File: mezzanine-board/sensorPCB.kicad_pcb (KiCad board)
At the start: 2 copper layers, 50.8 x 8 mm, 23 parts, among them J2 20021311-00020T4LF, U3 AS72652, U4 AS72653, U6 AS72651

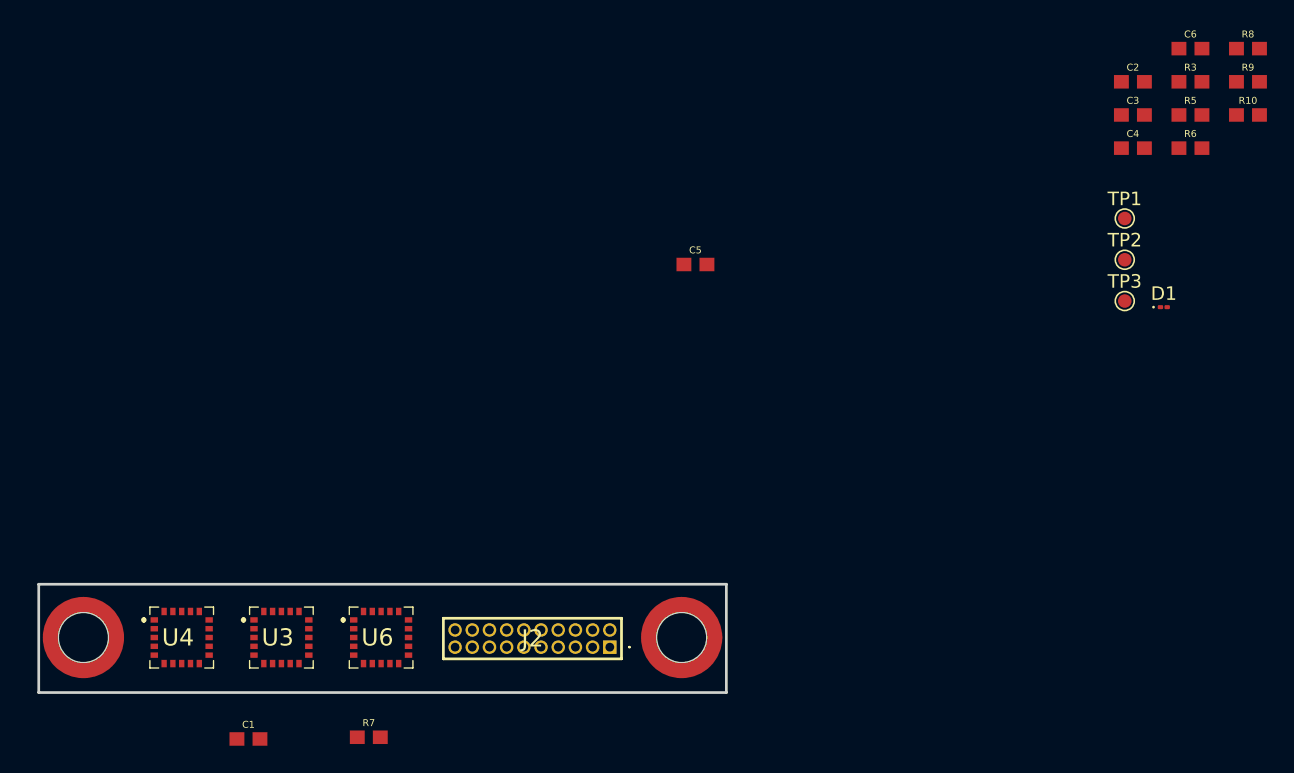
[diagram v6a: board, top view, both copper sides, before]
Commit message: Attach Raspberry Pi Zero 2 W 3D model to RPi footprint
Add the mechanical STEP model of the Raspberry Pi Zero 2 W board
(RaspberryPi_Zero_2W.step, from the downloaded SolidWorks CAD) to
main-board 3dmodels, and reference it from the RASPBERRYPI-ZERO_RPI-ZERO
footprint via a ${KIPRJMOD}-relative path. Offset/rotation set to zero as
a starting point - needs alignment tuning in KiCad's 3D tab.
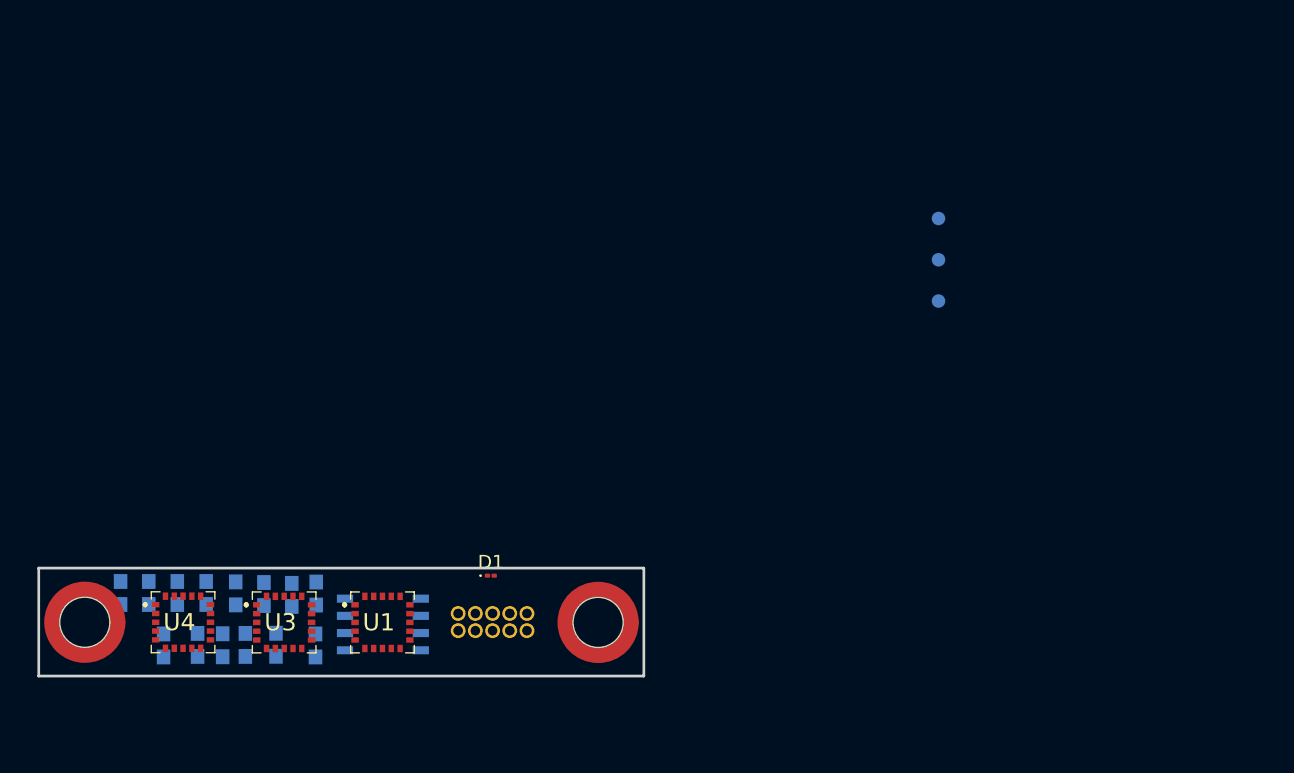
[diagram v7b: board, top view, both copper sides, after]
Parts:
- removed J2: 20021311-00020T4LF, SamacSys_Parts:2002131100020T4LF
- added C7: 1uF, SparkfunLibrary:0603, B.Cu at (109.4, 89.0)
- added J1: SFMC-105-01-L-D, SamacSys_Parts:SFMC-105-XX-YY-D, B.Cu at (119.9, 91.7)
- added U2: 4MB Flash, SparkfunLibrary:4MbFlash, B.Cu at (114.3, 91.2)
- C1, C2, C3, C6, TP1, TP2, TP3: moved to B.Cu
- C4: renamed from C5; moved to B.Cu
- C5: renamed from C4; moved to B.Cu
- R1: renamed from R3; moved to B.Cu
- R2: renamed from R6; moved to B.Cu
- R3: renamed from R5; moved to B.Cu
- R4: renamed from R7; moved to B.Cu
- R5: renamed from R8; moved to B.Cu
- R6: renamed from R9; moved to B.Cu
- R7: renamed from R10; moved to B.Cu
- moved R7 89.2 mm to (98.1, 92.8), turned to 90 degrees
- moved C6 88.7 mm to (94.9, 88.9), turned to 90 degrees
- moved R6 88.0 mm to (100.6, 92.7), turned to 90 degrees
- moved R5 87.6 mm to (102.5, 92.8), turned to 90 degrees
- moved C5 79.8 mm to (97.0, 88.9), turned to 90 degrees
- moved C3 77.0 mm to (101.3, 88.9), turned to 90 degrees
- moved R1 76.9 mm to (109.3, 92.8), turned to -90 degrees
- moved R2 76.9 mm to (106.4, 92.7), turned to 90 degrees
- moved R3 75.3 mm to (107.6, 89.1), turned to -90 degrees
- moved C2 74.5 mm to (105.5, 89.0), turned to 90 degrees
- moved D1 53.5 mm to (122.3, 87.6)
- moved C4 45.3 mm to (99.1, 88.9), turned to 90 degrees
- moved TP1 13.8 mm to (155.4, 61.2), turned to 180 degrees
- moved TP2 13.8 mm to (155.4, 64.3), turned to 180 degrees
- moved TP3 13.8 mm to (155.4, 67.3), turned to 180 degrees
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- renumbered U6 to U1
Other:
- board size 50.8 x 8 mm -> 44.7 x 8 mm

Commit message: Initial sensor board routing
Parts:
- removed TP1, TP2, TP3: TestPoint, TestPoint:TestPoint_Pad_D1.0mm
- R1, R2, R3: moved to F.Cu
- moved R3 23.0 mm to (130.0, 93.9), turned to 180 degrees
- moved R2 20.3 mm to (126.7, 93.6), turned to 0 degrees
- moved C7 13.1 mm to (96.3, 89.0)
- moved R1 12.3 mm to (121.2, 89.3), turned to 0 degrees
- moved D1 8.01 mm to (130.3, 87.9), turned to 180 degrees
- moved R4 6.30 mm to (108.5, 88.1), turned to 180 degrees
- moved R5 6.23 mm to (96.3, 93.1), turned to -90 degrees
- moved H2 5.08 mm to (135.3, 91.1)
- moved J1 4.70 mm to (124.6, 91.7)
- moved C6 2.85 mm to (97.8, 89.0)
- moved C5 2.29 mm to (99.3, 89.0)
- moved R6 2.07 mm to (98.9, 91.6), turned to 180 degrees
- moved U2 1.83 mm to (116.1, 90.7), turned to 90 degrees
- moved C4 1.71 mm to (100.8, 89.0)
- moved R7 1.44 mm to (98.9, 94.0), turned to 180 degrees
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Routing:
- net +3.3V: track 0.00 -> 106.7 mm, vias 0 -> 9
- net GND: track 0.00 -> 55.3 mm, vias 0 -> 5
- net INT: track 0.00 -> 35.4 mm, vias 0 -> 5
- net /SCL: track 0.00 -> 26.9 mm, vias 0 -> 2
- net SPI_SCK: track 0.00 -> 26.2 mm, vias 0 -> 1
- net /SLV1_RESN: track 0.00 -> 25.7 mm, vias 0 -> 1
- net SPI_MISO: track 0.00 -> 23.1 mm, vias 0 -> 3
- net /SDA: track 0.00 -> 22.0 mm, vias 0 -> 2
- net RESN: track 0.00 -> 21.7 mm, vias 0 -> 1
- net TX/SDA: track 0.00 -> 20.4 mm, vias 0 -> 1
- net SPI_MOSI: track 0.06 -> 19.2 mm, vias 0 -> 2
- net CSN_EE: track 0.00 -> 18.2 mm, vias 0 -> 2
- net I2C_ENA: track 0.00 -> 17.2 mm, vias 0 -> 2
- net Net-(D1-A): track 0.00 -> 15.0 mm, vias 0 -> 2
- net RX/SCL: track 0.00 -> 13.8 mm, vias 0 -> 1
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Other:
- board size 44.7 x 8 mm -> 50 x 8 mm
